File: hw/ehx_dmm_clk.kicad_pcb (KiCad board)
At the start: 2 copper layers, 39 parts, among them J1 Conn_01x06, J2 Conn_01x02, J3 Conn_01x02, J4 Conn_01x03, J5 Conn_01x02, J6 Conn_01x02, Q1 2N5401, Q2 2N5401, U1 PIC16F18326-P, U2 LM7905_TO220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

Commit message: Initial work on the PCBA layout
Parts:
- removed R3, R4, R7, R8: 10R, Resistor_THT:R_Axial_DIN0207_L6.3mm_D2.5mm_P7.62mm_Horizontal
- moved J6 116.2 mm to (90.2, 34.3)
- moved D2 105.0 mm to (105.4, 39.4), turned to 180 degrees
- moved C5 102.8 mm to (162.6, 33.0), turned to 180 degrees
- moved R13 90.1 mm to (108.0, 43.2), turned to 180 degrees
- moved R14 86.2 mm to (90.2, 50.8), turned to 90 degrees
- moved D1 83.0 mm to (149.9, 33.0), turned to 180 degrees
- moved U2 80.3 mm to (142.2, 40.6)
- moved J5 79.1 mm to (95.2, 111.8), turned to 180 degrees
- moved D3 78.9 mm to (94.0, 50.8), turned to 90 degrees
- moved J1 65.5 mm to (90.2, 68.6), turned to 180 degrees
- moved C1 60.6 mm to (130.8, 45.7), turned to 90 degrees
- moved Q2 60.4 mm to (118.1, 102.9)
- moved C4 58.6 mm to (158.8, 45.7), turned to 90 degrees
- moved C7 58.4 mm to (100.3, 69.8)
- moved Q1 54.4 mm to (118.1, 110.5)
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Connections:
- RV1 pad 1: Net-(R3-Pad2) -> GND
- RV1 pad 3: Net-(R4-Pad1) -> -5V
- RV2 pad 1: Net-(R7-Pad2) -> GND
- RV2 pad 3: Net-(R8-Pad1) -> -5V

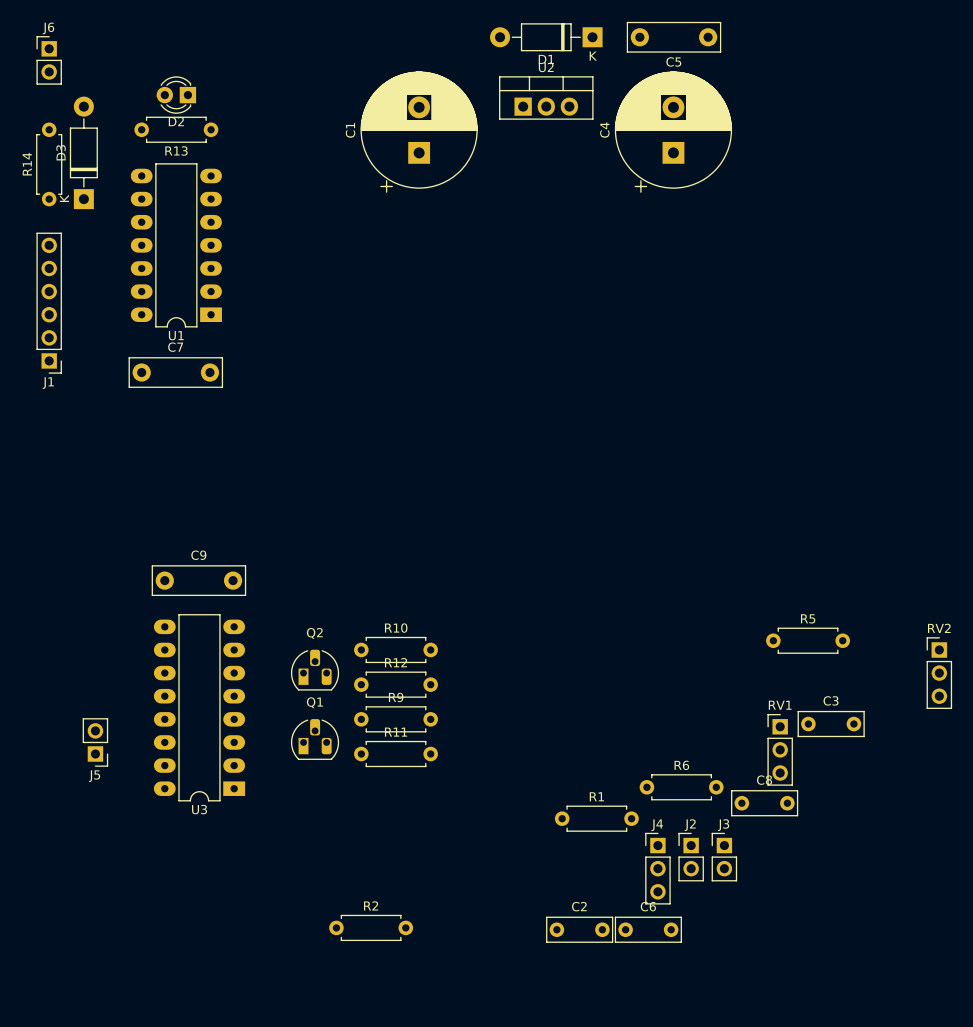
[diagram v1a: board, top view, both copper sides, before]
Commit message: Initial PCB floorplanning complete
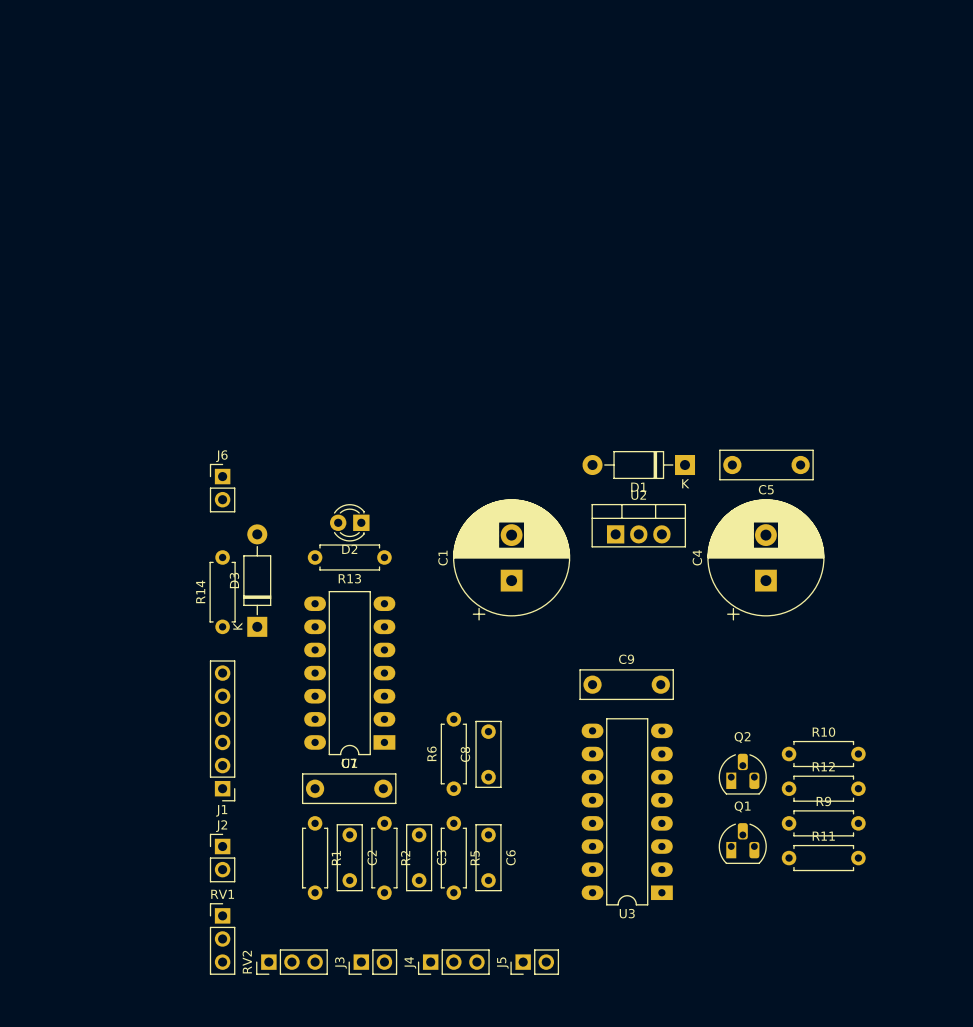
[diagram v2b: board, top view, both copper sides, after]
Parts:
- moved RV2 81.3 mm to (114.3, 134.6), turned to 90 degrees
- moved RV1 64.7 mm to (109.2, 129.5)
- moved J5 52.3 mm to (142.2, 134.6), turned to 90 degrees
- moved J2 51.5 mm to (109.2, 121.9)
- moved D3 50.7 mm to (113.0, 97.8)
- moved R14 50.7 mm to (109.2, 97.8)
- moved D2 50.7 mm to (124.5, 86.4)
- moved J6 50.7 mm to (109.2, 81.3)
- moved R13 50.7 mm to (127.0, 90.2)
- moved J1 50.7 mm to (109.2, 115.6)
- moved U1 50.7 mm to (127.0, 110.5)
- moved C7 49.5 mm to (119.4, 115.6)
- moved C9 48.4 mm to (149.9, 104.1)
- moved Q1 48.4 mm to (165.1, 121.9)
- moved Q2 48.4 mm to (165.1, 114.3)
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
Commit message: Added some mounting holes
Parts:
- added H1: MountingHole, MountingHole:MountingHole_3mm, F.Cu at (122.4, 41.1)
- added H2: MountingHole, MountingHole:MountingHole_3mm, F.Cu at (122.4, 49.7)
- added H3: MountingHole, MountingHole:MountingHole_3mm, F.Cu at (130.9, 41.1)
- added H4: MountingHole, MountingHole:MountingHole_3mm, F.Cu at (130.9, 49.7)
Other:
- board outline added: 78.7 x 63.5 mm
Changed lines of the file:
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@@
   (general
     (thickness 1.6)
-    (drawings 0)
+    (drawings 4)
     (tracks 0)
     (zones 0)
-    (modules 35)
+    (modules 39)
     (nets 28)
   )
@@
     (add_net "Net-(U3-Pad15)")
     (add_net "Net-(U3-Pad6)")
+  )
+  (module MountingHole:MountingHole_3mm (layer F.Cu)
+    (at 122.385001 41.105001)
+    (descr "Mounting Hole 3mm, no annular")
+    (tags "mounting hole 3mm no annular")
+    (attr virtual)
+    (fp_text reference H1 (at 0 -4) (layer F.SilkS)
+      (effects (font (size 1 1) (thickness 0.15)))
+    )
+    (fp_text value MountingHole (at 0 4) (layer F.Fab)
+      (effects (font (size 1 1) (thickness 0.15)))
+    )
+    (fp_circle (center 0 0) (end 3.25 0) (layer F.CrtYd) (width 0.05))
+    (fp_circle (center 0 0) (end 3 0) (layer Cmts.User) (width 0.15))
+    (fp_text user %R (at 0.3 0) (layer F.Fab)
+      (effects (font (size 1 1) (thickness 0.15)))
+    )
+    (pad 1 np_thru_hole circle (at 0 0) (size 3 3) (drill 3) (layers *.Cu *.Mask))
+  )
+  (module MountingHole:MountingHole_3mm (layer F.Cu)
+    (at 122.385001 49.655001)
+    (descr "Mounting Hole 3mm, no annular")
+    (tags "mounting hole 3mm no annular")
+    (attr virtual)
+    (fp_text reference H2 (at 0 -4) (layer F.SilkS)
+      (effects (font (size 1 1) (thickness 0.15)))
+    )
+    (fp_text value MountingHole (at 0 4) (layer F.Fab)
+      (effects (font (size 1 1) (thickness 0.15)))
+    )
+    (fp_text user %R (at 0.3 0) (layer F.Fab)
+      (effects (font (size 1 1) (thickness 0.15)))
+    )
+    (fp_circle (center 0 0) (end 3 0) (layer Cmts.User) (width 0.15))
+    (fp_circle (center 0 0) (end 3.25 0) (layer F.CrtYd) (width 0.05))
+    (pad 1 np_thru_hole circle (at 0 0) (size 3 3) (drill 3) (layers *.Cu *.Mask))
+  )
+  (module MountingHole:MountingHole_3mm (layer F.Cu)
+    (at 130.935001 49.655001)
+    (descr "Mounting Hole 3mm, no annular")
+    (tags "mounting hole 3mm no annular")
+    (attr virtual)
+    (fp_text reference H4 (at 0 -4) (layer F.SilkS)
+      (effects (font (size 1 1) (thickness 0.15)))
+    )
+    (fp_text value MountingHole (at 0 4) (layer F.Fab)
+      (effects (font (size 1 1) (thickness 0.15)))
+    )
+    (fp_circle (center 0 0) (end 3.25 0) (layer F.CrtYd) (width 0.05))
+    (fp_circle (center 0 0) (end 3 0) (layer Cmts.User) (width 0.15))
+    (fp_text user %R (at 0.3 0) (layer F.Fab)
+      (effects (font (size 1 1) (thickness 0.15)))
+    )
+    (pad 1 np_thru_hole circle (at 0 0) (size 3 3) (drill 3) (layers *.Cu *.Mask))
+  )
+  (module MountingHole:MountingHole_3mm (layer F.Cu)
+    (at 130.935001 41.105001)
+    (descr "Mounting Hole 3mm, no annular")
+    (tags "mounting hole 3mm no annular")
+    (attr virtual)
+    (fp_text reference H3 (at 0 -4) (layer F.SilkS)
+      (effects (font (size 1 1) (thickness 0.15)))
+    )
+    (fp_text value MountingHole (at 0 4) (layer F.Fab)
+      (effects (font (size 1 1) (thickness 0.15)))
+    )
+    (fp_text user %R (at 0.3 0) (layer F.Fab)
+      (effects (font (size 1 1) (thickness 0.15)))
+    )
+    (fp_circle (center 0 0) (end 3 0) (layer Cmts.User) (width 0.15))
+    (fp_circle (center 0 0) (end 3.25 0) (layer F.CrtYd) (width 0.05))
+    (pad 1 np_thru_hole circle (at 0 0) (size 3 3) (drill 3) (layers *.Cu *.Mask))
   )
   (module Capacitor_THT:CP_Radial_D12.5mm_P5.00mm (layer F.Cu)
@@
     )
   )
+  (gr_line (start 102.87 139.7) (end 102.87 76.2) (layer Edge.Cuts) (width 0.15))
+  (gr_line (start 181.61 139.7) (end 102.87 139.7) (layer Edge.Cuts) (width 0.15))
+  (gr_line (start 181.61 76.2) (end 181.61 139.7) (layer Edge.Cuts) (width 0.15))
+  (gr_line (start 102.87 76.2) (end 181.61 76.2) (layer Edge.Cuts) (width 0.15))
 )

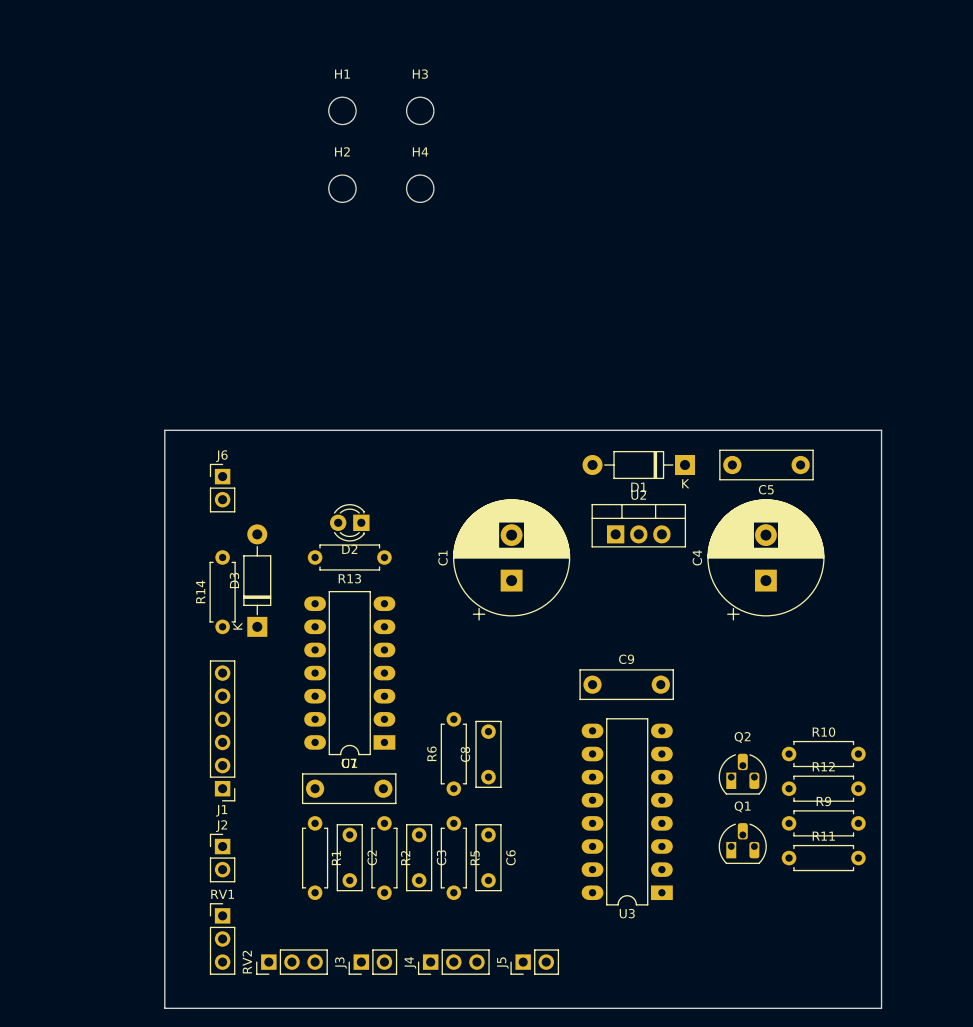
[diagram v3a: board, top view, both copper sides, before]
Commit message: Huge commit. Major changes to board size, layout, footprints, etc. All to get the design to fit into the enclosure
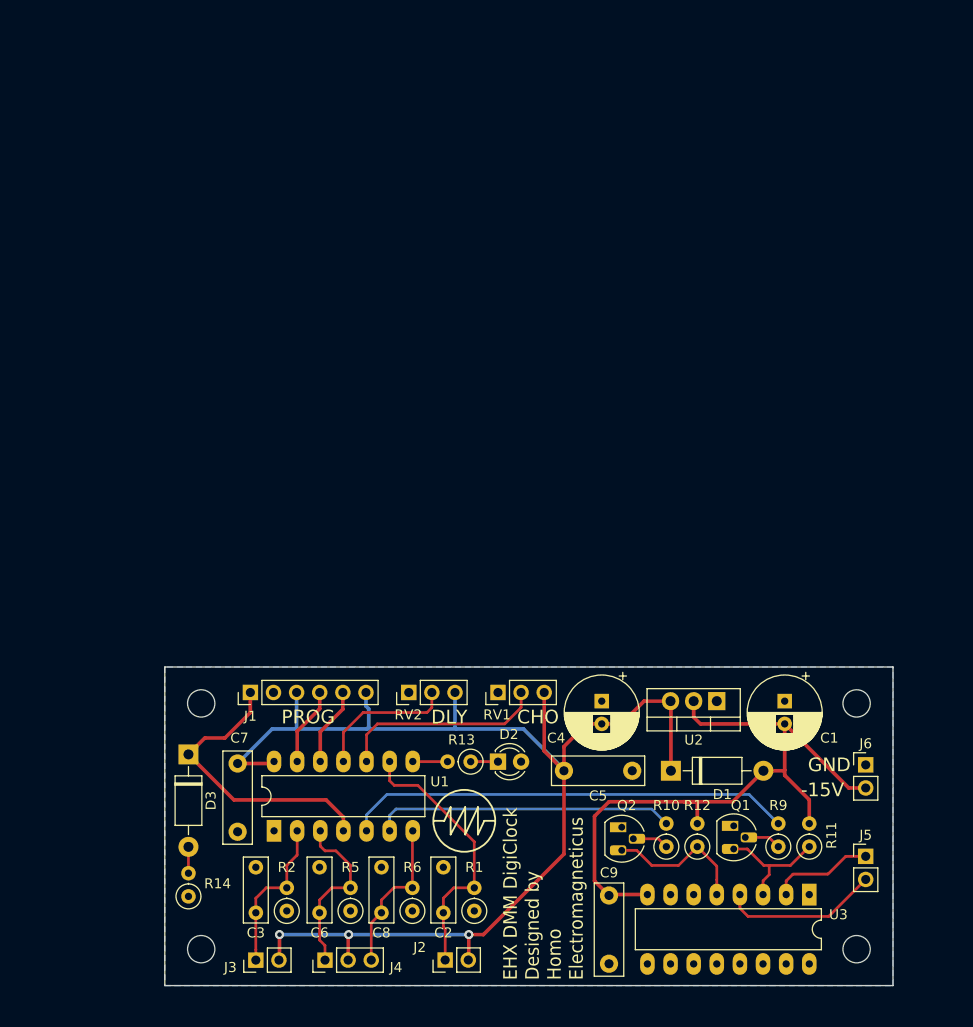
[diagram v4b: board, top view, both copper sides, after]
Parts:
- C1, C4: footprint Capacitor_THT:CP_Radial_D12.5mm_P5.00mm -> Capacitor_THT:CP_Radial_D8.0mm_P2.50mm
- R1, R10, R11, R12, R13, R14, R2, R5, R6, R9: footprint Resistor_THT:R_Axial_DIN0207_L6.3mm_D2.5mm_P7.62mm_Horizontal -> Resistor_THT:R_Axial_DIN0207_L6.3mm_D2.5mm_P2.54mm_Vertical
- moved H4 96.3 mm to (178.9, 133.2)
- moved H3 95.2 mm to (106.9, 133.2)
- moved H2 79.9 mm to (178.9, 106.2)
- moved J6 77.4 mm to (179.9, 113.0)
- moved H1 66.9 mm to (106.9, 106.2)
- moved J5 39.4 mm to (179.9, 123.0), turned to 0 degrees
- moved RV1 39.0 mm to (139.5, 105.0), turned to 90 degrees
- moved C5 38.3 mm to (154.2, 113.6)
- moved D1 33.6 mm to (158.5, 113.6), turned to 0 degrees
- moved RV2 33.4 mm to (129.7, 105.0)
- moved C1 32.8 mm to (171.0, 106.0), turned to 270 degrees
- moved C9 30.7 mm to (151.7, 134.8), turned to 90 degrees
- moved D2 30.2 mm to (139.5, 112.6), turned to 0 degrees
- moved R14 29.8 mm to (105.5, 127.4)
- moved J2 27.4 mm to (133.7, 134.4), turned to 90 degrees
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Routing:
- net -5V: track 0.00 -> 142.7 mm, vias 0 -> 3
- net -15V: track 0.00 -> 76.6 mm
- net /LV_BBD_CLK: track 0.00 -> 49.3 mm
- net /~LV_BBD_CLK: track 0.00 -> 33.0 mm
- net /~MCLR~\VPP: track 0.00 -> 32.3 mm
- net /TAP_TEMPO: track 0.00 -> 30.3 mm
- net /CHORUS_AMOUNT: track 0.00 -> 22.8 mm
- net /DOTTED: track 0.00 -> 20.4 mm
- net /DBL_TIME: track 0.00 -> 17.6 mm
- net /~BBD_CLK: track 0.00 -> 17.4 mm
- net /TRIPLET: track 0.00 -> 17.3 mm
- net Net-(Q2-Pad3): track 0.00 -> 16.0 mm
- net /DELAY_TIME: track 0.00 -> 15.7 mm
- net Net-(Q1-Pad3): track 0.00 -> 13.4 mm
- net /BBD_CLK: track 0.00 -> 11.4 mm
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- added copper zone on B.Cu, net GND
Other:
- board size 78.7 x 63.5 mm -> 80 x 35 mm
- net class Default: clearance 0.2 -> 0.3; trace_width 0.25 -> 0.3; via_dia 0.8 -> 1; via_drill 0.4 -> 0.5
- rule pad_to_mask_clearance: 0.051 -> 0.15
- rule trace_clearance: 0.2 -> 0.3
- board text added: "-15V"
- board text added: "CHO"
- board text added: "DLY"
- board text added: "EHX DMM DigiClock Designed by Homo Electromagneticus"
- board text added: "GND"
- board text added: "PROG"
